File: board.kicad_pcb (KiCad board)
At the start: 2 copper layers, 92 x 72 mm, 50 parts, among them J1 Z, J10 CNC/Laser, J11 Conn_01x03_Male, J12 12V, J13 Y, J14 X, J15 12V-36V, J16 CNC_OUT2, J2 Pololu_Breakout_A4988, J3 Y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

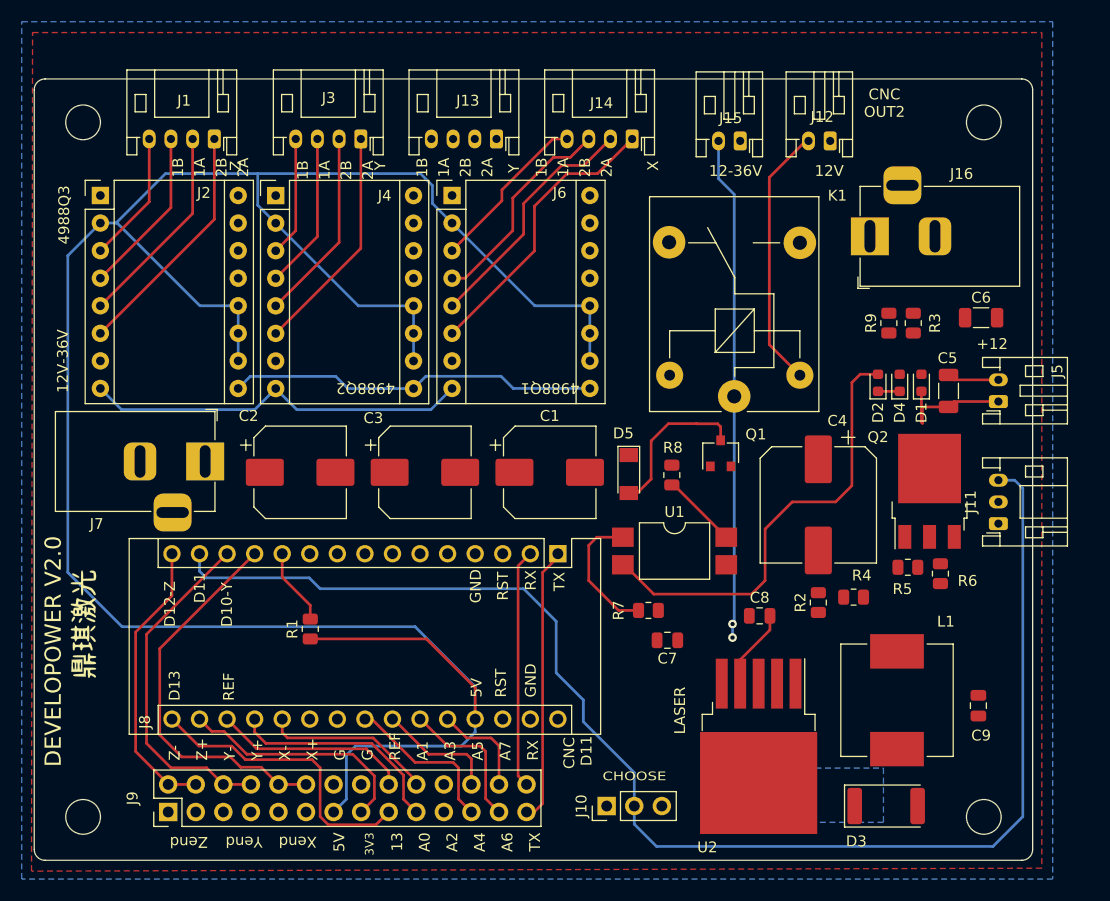
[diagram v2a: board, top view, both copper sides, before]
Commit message: Connect extra signals, 90% done
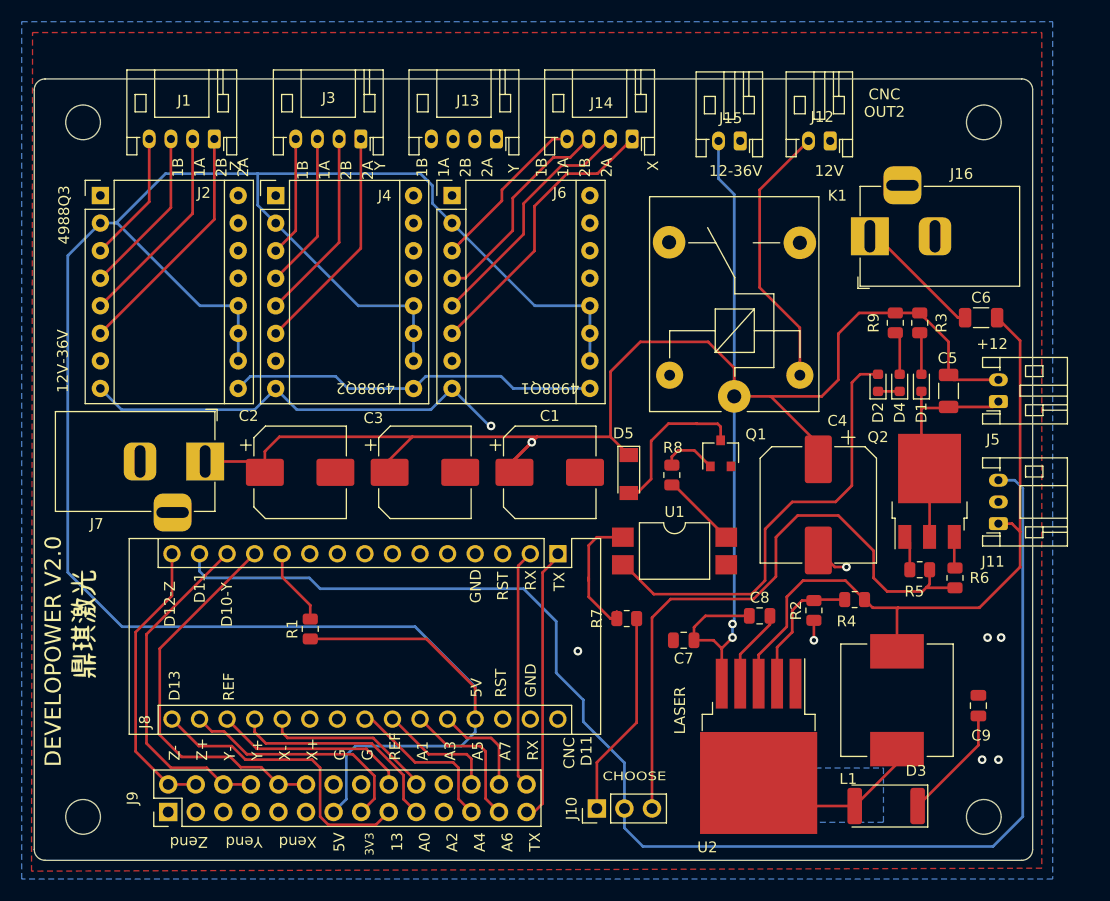
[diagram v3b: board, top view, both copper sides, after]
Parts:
- D5: value LED -> MELF
- J10: value CNC/Laser -> Mode
- moved R7 2.14 mm to (158.8, 113.0)
- moved C7 1.50 mm to (164.0, 115.0)
- moved R6 1.40 mm to (189.0, 109.2), turned to 270 degrees
- moved R5 1.12 mm to (185.8, 108.5)
- moved J10 0.93 mm to (156.0, 130.5)
- moved R2 0.83 mm to (176.0, 112.2)
- moved R3 0.59 mm to (185.8, 85.8), turned to 270 degrees
- moved R9 0.59 mm to (183.5, 85.8), turned to 270 degrees
- moved R4 0.24 mm to (179.8, 111.2), turned to 180 degrees
- turned D3 to 180 degrees
- turned L1 to 270 degrees
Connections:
- C1 pad 1: (no net) -> +12V
- C2 pad 1: (no net) -> +12V
- C3 pad 1: (no net) -> +12V
- C4 pad 1: (no net) -> +12V
- C5 pad 1: GND -> Net-(C5-Pad1)
- C5 pad 2: Net-(C5-Pad2) -> +12V
- C6 pad 1: (no net) -> /XXXX
- C6 pad 2: GND -> Net-(C6-Pad2)
- C7 pad 1: Net-(C7-Pad1) -> +12V
- C8 pad 1: GND -> +12V
- C8 pad 2: Net-(C7-Pad1) -> Net-(C8-Pad2)
- C9 pad 1: (no net) -> Net-(C9-Pad1)
- D1 pad 1: GND -> Net-(C5-Pad1)
- D3 pad 1: (no net) -> Net-(C9-Pad1)
- D5 pad 1: (no net) -> +12V
- J10 pad 1: (no net) -> /CNC
- J10 pad 3: (no net) -> /LASER
- J12 pad 2: /relay.p2 -> /VMOT
- J15 pad 2: /relay.common -> +12V
- J16 pad 1: (no net) -> Net-(C6-Pad2)
- J5 pad 1: GND -> Net-(C5-Pad1)
- J5 pad 2: Net-(C5-Pad2) -> +12V
- J7 pad 1: (no net) -> +12V
- K1 pad 1: /relay.common -> +12V
- K1 pad 2: /relay.p2 -> /VMOT
- L1 pad 1: (no net) -> /XXXX
- L1 pad 2: (no net) -> Net-(D3-Pad2)
- Q1 pad 1: (no net) -> Net-(Q1-Pad1)
- Q2 pad 1: (no net) -> Net-(Q2-Pad1)
- Q2 pad 2: Net-(Q2-Pad2) -> Net-(C5-Pad1)
- Q2 pad 3: (no net) -> Net-(Q2-Pad3)
- R2 pad 1: (no net) -> GND
- R2 pad 2: (no net) -> /XXXX
- R3 pad 1: Net-(C5-Pad2) -> +12V
- R4 pad 1: (no net) -> Net-(R4-Pad1)
- R4 pad 2: (no net) -> /XXXX
- R5 pad 1: (no net) -> Net-(Q2-Pad1)
- R5 pad 2: (no net) -> /LASER
- R6 pad 1: (no net) -> Net-(Q2-Pad3)
- R6 pad 2: (no net) -> /LASER
- R7 pad 1: (no net) -> /CNC
- R8 pad 1: (no net) -> Net-(Q1-Pad1)
- R9 pad 1: Net-(C5-Pad2) -> +12V
- U2 pad 2: (no net) -> /XXXX
- U2 pad 3: (no net) -> Net-(R4-Pad1)
- U2 pad 4: Net-(C7-Pad1) -> Net-(C8-Pad2)
- U2 pad 5: (no net) -> +12V
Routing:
- net +12V: track 0.00 -> 178.3 mm, vias 0 -> 3
- net /XXXX: track 0.00 -> 76.6 mm
- net /LASER: track 0.00 -> 58.0 mm
- net /relay.common: track 46.7 -> 0.00 mm, vias 2 -> 0
- net /VMOT: track 35.6 -> 65.6 mm, vias 0 -> 1
- net /relay.p2: track 24.5 -> 0.00 mm
- net Net-(C5-Pad1): track 0.00 -> 21.1 mm
- net /CNC: track 0.00 -> 19.0 mm
- net Net-(D3-Pad2): track 0.00 -> 16.6 mm
- net /12v_VOLTAGE: track 0.00 -> 11.9 mm
- net Net-(C9-Pad1): track 0.00 -> 10.6 mm
- net Net-(C8-Pad2): track 0.00 -> 9.59 mm
- net Net-(C7-Pad1): track 7.39 -> 0.00 mm
- net GND: track 13.7 -> 7.06 mm, vias 0 -> 7
- net Net-(Q1-Pad1): track 0.00 -> 5.17 mm
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
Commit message: Improve connections
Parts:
- J11: value Conn_01x03_Male -> V_LASER
- J5: value 12-36V -> LASER
- L1: value 470 -> 47u/5A
- turned C6 to 180 degrees
- turned C8 to 180 degrees
- turned C9 to 270 degrees
- turned D3 to 0 degrees
- turned L1 to 90 degrees
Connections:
- net /CNC renamed /SPINDLE
- net /X.1A renamed Net-(J14-Pad3)
- net /X.1B renamed Net-(J14-Pad4)
- net /X.2A renamed Net-(J14-Pad2)
- net /X.2B renamed Net-(J14-Pad1)
- net /Z.1A renamed Net-(J1-Pad3)
- net /Z.1B renamed Net-(J1-Pad4)
- net /Z.2A renamed Net-(J1-Pad2)
- net /Z.2B renamed Net-(J1-Pad1)
- C1 pad 1: +12V -> /V_STEP_MOT
- C2 pad 1: +12V -> /V_STEP_MOT
- C3 pad 1: +12V -> /V_STEP_MOT
- C4 pad 1: +12V -> 12V_36V
- C5 pad 2: +12V -> /V_LASER
- C6 pad 1: /XXXX -> GND
- C6 pad 2: Net-(C6-Pad2) -> /V_SPINDLE
- C7 pad 1: +12V -> 12V_36V
- C8 pad 1: +12V -> Net-(C8-Pad1)
- C8 pad 2: Net-(C8-Pad2) -> 12V_36V
- C9 pad 1: Net-(C9-Pad1) -> /V_LASER
- D3 pad 1: Net-(C9-Pad1) -> Net-(D3-Pad1)
- D3 pad 2: Net-(D3-Pad2) -> GND
- D5 pad 1: +12V -> /V_STEP_MOT
- J11 pad 1: (no net) -> /V_LASER
- J12 pad 2: /VMOT -> (no net)
- J13 pad 1: (no net) -> Net-(J13-Pad1)
- J13 pad 2: (no net) -> Net-(J13-Pad2)
- J13 pad 3: (no net) -> Net-(J13-Pad3)
- J13 pad 4: (no net) -> Net-(J13-Pad4)
- J15 pad 2: +12V -> 12V_36V
- J16 pad 1: Net-(C6-Pad2) -> /V_SPINDLE
- J2 pad 13: (no net) -> Net-(J2-Pad13)
- J2 pad 14: (no net) -> Net-(J2-Pad13)
- J2 pad 15: (no net) -> /D4
- J2 pad 16: (no net) -> /D7
- J2 pad 8: /VMOT -> /V_STEP_MOT
- J2 pad 9: /EN -> /D8
- J3 pad 1: /Y.2B -> Net-(J13-Pad4)
- J3 pad 2: /Y.2A -> Net-(J13-Pad3)
- J3 pad 3: /Y.1A -> Net-(J13-Pad2)
- J3 pad 4: /Y.1B -> Net-(J13-Pad1)
- J4 pad 13: (no net) -> Net-(J4-Pad13)
- J4 pad 14: (no net) -> Net-(J4-Pad13)
- J4 pad 15: (no net) -> /D3
- J4 pad 16: (no net) -> /D6
- J4 pad 3: /Y.1B -> Net-(J13-Pad1)
- J4 pad 4: /Y.1A -> Net-(J13-Pad2)
- J4 pad 5: /Y.2A -> Net-(J13-Pad3)
- J4 pad 6: /Y.2B -> Net-(J13-Pad4)
- J4 pad 8: /VMOT -> /V_STEP_MOT
- J4 pad 9: /EN -> /D8
- J5 pad 2: +12V -> /V_LASER
- J6 pad 13: (no net) -> Net-(J6-Pad13)
- J6 pad 14: (no net) -> Net-(J6-Pad13)
- J6 pad 15: (no net) -> /D2
- J6 pad 16: (no net) -> /D5
- J6 pad 8: /VMOT -> /V_STEP_MOT
- J6 pad 9: /EN -> /D8
- J7 pad 1: +12V -> (no net)
- J8 pad 10: (no net) -> /D7
- J8 pad 5: (no net) -> /D2
- J8 pad 6: (no net) -> /D3
- J8 pad 7: (no net) -> /D4
- J8 pad 8: (no net) -> /D5
- J8 pad 9: (no net) -> /D6
- K1 pad 1: +12V -> 12V_36V
- K1 pad 2: /VMOT -> /V_STEP_MOT
- K1 pad 3: (no net) -> /V_SPINDLE
- L1 pad 1: /XXXX -> Net-(D3-Pad1)
- L1 pad 2: Net-(D3-Pad2) -> /V_LASER
- R2 pad 2: /XXXX -> Net-(R2-Pad2)
- R3 pad 1: +12V -> /V_LASER
- R4 pad 1: Net-(R4-Pad1) -> /V_LASER
- R4 pad 2: /XXXX -> Net-(R2-Pad2)
- R9 pad 1: +12V -> /V_LASER
- U2 pad 2: /XXXX -> Net-(R2-Pad2)
- U2 pad 3: Net-(R4-Pad1) -> Net-(D3-Pad1)
- U2 pad 4: Net-(C8-Pad2) -> Net-(C8-Pad1)
- U2 pad 5: +12V -> 12V_36V
- U2 pad 6: Net-(D3-Pad2) -> Net-(D3-Pad1)
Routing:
- net +12V: track 178.3 -> 0.00 mm, vias 3 -> 0
- net /V_STEP_MOT: track 0.00 -> 142.8 mm, vias 0 -> 3
- net /XXXX: track 76.6 -> 0.00 mm
- net /V_LASER: track 0.00 -> 74.5 mm
- net 12V_36V: track 0.00 -> 71.9 mm, vias 0 -> 2
- net /VMOT: track 65.6 -> 0.00 mm, vias 1 -> 0
- net Net-(J13-Pad1): track 0.00 -> 35.1 mm
- net /EN: track 34.3 -> 0.00 mm
- net /D8: track 7.09 -> 41.4 mm
- net Net-(J13-Pad2): track 0.00 -> 33.2 mm
- net Net-(J13-Pad3): track 0.00 -> 31.2 mm
- net Net-(J13-Pad4): track 0.00 -> 27.7 mm
- net Net-(D3-Pad1): track 0.00 -> 25.7 mm
- net /Y.2B: track 21.2 -> 0.00 mm
- net /V_SPINDLE: track 0.00 -> 18.6 mm
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
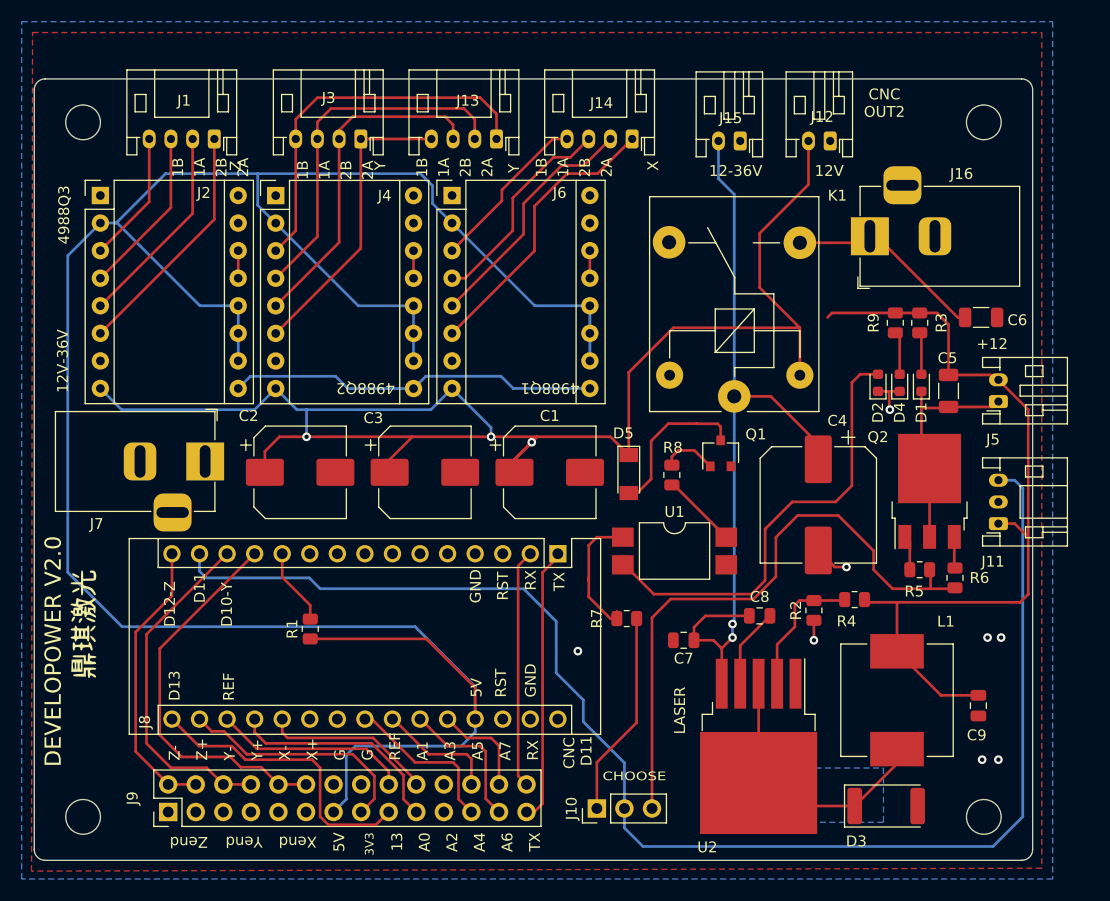
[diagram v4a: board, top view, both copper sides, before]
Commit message: Update some parts
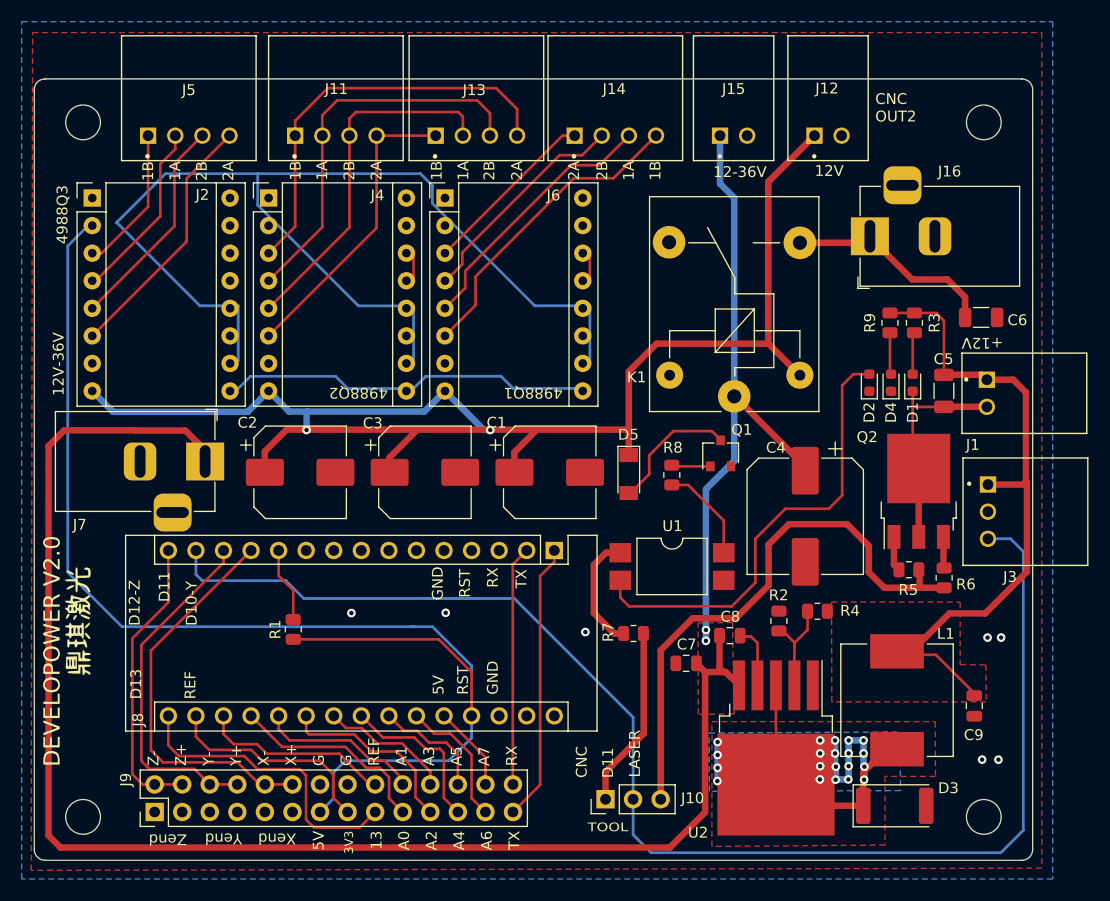
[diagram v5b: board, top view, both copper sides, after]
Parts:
- J1: value Z -> LASER; footprint Connector_JST:JST_PH_S4B-PH-K_1x04_P2.00mm_Horizontal -> Developower:JST_S2B-XH-A(LF)(SN)
- J11: renamed from J3; footprint Connector_JST:JST_PH_S4B-PH-K_1x04_P2.00mm_Horizontal -> Developower:JST_S4B-XH-A(LF)(SN)
- J12, J15: footprint Connector_JST:JST_PH_S2B-PH-K_1x02_P2.00mm_Horizontal -> Developower:JST_S2B-XH-A(LF)(SN)
- J13, J14: footprint Connector_JST:JST_PH_S4B-PH-K_1x04_P2.00mm_Horizontal -> Developower:JST_S4B-XH-A(LF)(SN)
- J3: renamed from J11; footprint Connector_JST:JST_PH_S3B-PH-K_1x03_P2.00mm_Horizontal -> Developower:JST_S3B-XH-A(LF)(SN)
- J5: value LASER -> Z; footprint Connector_JST:JST_PH_S2B-PH-K_1x02_P2.00mm_Horizontal -> Developower:JST_S4B-XH-A(LF)(SN)
- K1: value SANYOU_SRD_Form_C -> SRD-12VDC-SL-C; footprint Relay_THT:Relay_SPDT_SANYOU_SRD_Series_Form_C -> Developower:Relay_SPDT_SANYOU_SRD_Series_Form_C
- L1: footprint Inductor_SMD:L_Vishay_IHLP-4040 -> Developower:L_Vishay_IHLP-4040
- moved J5 78.5 mm to (118.4, 68.5), turned to 0 degrees
- moved J1 74.9 mm to (191.9, 92.2), turned to 270 degrees
- moved R4 3.59 mm to (176.3, 112.3)
- moved R2 3.37 mm to (172.8, 113.2), turned to 270 degrees
- moved C8 3.30 mm to (168.2, 114.6)
- moved J3 2.72 mm to (195.5, 103.2), turned to 270 degrees
- moved J11 2.32 mm to (131.9, 68.5), turned to 0 degrees
- moved C7 2.14 mm to (164.2, 117.1)
- moved J13 1.88 mm to (144.9, 68.5), turned to 0 degrees
- moved U2 1.60 mm to (172.5, 124.9)
- moved C4 1.60 mm to (175.2, 103.6)
- moved J14 1.58 mm to (157.7, 68.5), turned to 0 degrees
- moved R1 1.57 mm to (128.0, 114.0)
- moved R7 1.51 mm to (159.4, 114.4)
- moved U1 1.44 mm to (162.9, 108.2)
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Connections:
- J1 pad 1: Net-(J1-Pad1) -> /V_LASER
- J1 pad 2: Net-(J1-Pad2) -> Net-(C5-Pad1)
- J11 pad 1: Net-(J13-Pad4) -> Net-(J11-Pad1)
- J11 pad 2: Net-(J13-Pad3) -> Net-(J11-Pad2)
- J11 pad 3: Net-(J13-Pad2) -> Net-(J11-Pad3)
- J11 pad 4: Net-(J13-Pad1) -> Net-(J11-Pad4)
- J12 pad 1: GND -> /V_STEP_MOT
- J12 pad 2: (no net) -> GND
- J13 pad 1: Net-(J13-Pad1) -> Net-(J11-Pad4)
- J13 pad 2: Net-(J13-Pad2) -> Net-(J11-Pad3)
- J13 pad 3: Net-(J13-Pad3) -> Net-(J11-Pad2)
- J13 pad 4: Net-(J13-Pad4) -> Net-(J11-Pad1)
- J15 pad 1: GND -> 12V_36V
- J15 pad 2: 12V_36V -> GND
- J2 pad 3: Net-(J1-Pad4) -> Net-(J2-Pad3)
- J2 pad 4: Net-(J1-Pad3) -> Net-(J2-Pad4)
- J2 pad 5: Net-(J1-Pad2) -> Net-(J2-Pad5)
- J2 pad 6: Net-(J1-Pad1) -> Net-(J2-Pad6)
- J4 pad 3: Net-(J13-Pad1) -> Net-(J11-Pad1)
- J4 pad 4: Net-(J13-Pad2) -> Net-(J11-Pad2)
- J4 pad 5: Net-(J13-Pad3) -> Net-(J11-Pad3)
- J4 pad 6: Net-(J13-Pad4) -> Net-(J11-Pad4)
- J5 pad 1: Net-(C5-Pad1) -> Net-(J2-Pad3)
- J5 pad 2: /V_LASER -> Net-(J2-Pad4)
- J6 pad 3: Net-(J14-Pad4) -> Net-(J14-Pad1)
- J6 pad 4: Net-(J14-Pad3) -> Net-(J14-Pad2)
- J6 pad 5: Net-(J14-Pad2) -> Net-(J14-Pad3)
- J6 pad 6: Net-(J14-Pad1) -> Net-(J14-Pad4)
- J7 pad 1: (no net) -> 12V_36V
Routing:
- net 12V_36V: track 71.9 -> 195.7 mm
- net Net-(J11-Pad1): track 0.00 -> 38.2 mm
- net Net-(J11-Pad2): track 0.00 -> 35.9 mm
- net Net-(J13-Pad1): track 35.1 -> 0.00 mm
- net Net-(J13-Pad2): track 33.2 -> 0.00 mm
- net Net-(J11-Pad3): track 0.00 -> 33.2 mm
- net Net-(J13-Pad3): track 31.2 -> 0.00 mm
- net Net-(J11-Pad4): track 0.00 -> 28.0 mm
- net Net-(J13-Pad4): track 27.7 -> 0.00 mm
- net Net-(J2-Pad6): track 0.00 -> 23.7 mm
- net Net-(J1-Pad1): track 22.3 -> 0.00 mm
- net Net-(D3-Pad1): track 25.7 -> 47.6 mm, vias 0 -> 20
- net Net-(J2-Pad5): track 0.00 -> 20.1 mm
- net Net-(J1-Pad2): track 18.9 -> 0.00 mm
- net /A2: track 0.00 -> 17.4 mm
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- added copper zone on F.Cu, net /V_LASER
- added copper zone on F.Cu, net 12V_36V
- added copper zone on B.Cu, net Net-(D3-Pad1)
- added copper zone on F.Cu, net Net-(D3-Pad1)
- removed copper zone on B.Cu, net (none)
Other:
- net class Power added: clearance 0.6, trace_width 0.6, via_dia 0.8, via_drill 0.4
- board text added: "+12V"
- board text added: "TOOL"
- board text removed: "CHOOSE"

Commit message: Add missing connection to the GND
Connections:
- Q2 pad 3: Net-(Q2-Pad3) -> GND
- R6 pad 1: Net-(Q2-Pad3) -> GND
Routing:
- net Net-(Q2-Pad3): track 2.89 -> 0.00 mm
- net GND: track 0.00 -> 2.89 mm

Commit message: Fix n-mosfet symbol/footprint and improve circuit
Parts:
- Q2: footprint Package_TO_SOT_SMD:TO-252-3_TabPin2 -> Package_TO_SOT_SMD:TO-252-2
- moved Q2 0.33 mm to (185.7, 101.6)
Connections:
- C5 pad 1: Net-(C5-Pad1) -> /V_LASER
- C5 pad 2: /V_LASER -> Net-(C5-Pad2)
- D1 pad 1: Net-(C5-Pad1) -> Net-(C5-Pad2)
- J1 pad 2: Net-(C5-Pad1) -> Net-(C5-Pad2)
- Q2 pad 2: Net-(C5-Pad1) -> Net-(C5-Pad2)
- R6 pad 1: GND -> /LASER
- R6 pad 2: /LASER -> GND
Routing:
- net Net-(C5-Pad1): track 21.7 -> 14.3 mm
- net /LASER: track 52.9 -> 55.8 mm
- net GND: track 2.89 -> 0.00 mm
- net Net-(Q2-Pad1): track 3.87 -> 3.22 mm

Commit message: Update Q1
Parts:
- moved Q1 1.87 mm to (165.6, 98.3)
- moved R8 1.36 mm to (162.3, 98.6)
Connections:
- D5 pad 2: Net-(D5-Pad2) -> /relay.p5
- K1 pad 5: (no net) -> /relay.p5
- Q1 pad 3: Net-(D5-Pad2) -> /relay.p5
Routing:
- net /relay.p5: track 0.00 -> 16.5 mm
- net Net-(D5-Pad2): track 12.2 -> 0.00 mm
- net Net-(Q1-Pad1): track 4.02 -> 3.12 mm
